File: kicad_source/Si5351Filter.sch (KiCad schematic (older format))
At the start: 31 parts, among them CN1 CON-SMA-EDGE-S-ND, CN2 CON-SMA-EDGE-S-ND, CN3 CON-SMA-EDGE-S-ND, CN4 CON-SMA-EDGE-S-ND, CN5 CON-SMA-EDGE-S-ND, CN6 CON-SMA-EDGE-S-ND

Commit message: added dual footprint for big and small SMA connectors
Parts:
- CN1, CN2, CN3, CN4, CN5, CN6: footprint CON_wuerth:WR-SMA-PCB -> CON_wuerth:WR-SMA-PCB_dual
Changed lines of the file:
@@
 F 0 "CN2" H 6572 1575 60  0000 R CNN
 F 1 "CON-SMA-EDGE-S-ND " H 6572 1469 60  0000 R CNN
-F 2 "CON_wuerth:WR-SMA-PCB" H 6572 1469 60  0001 R CNN
+F 2 "CON_wuerth:WR-SMA-PCB_dual" H 6572 1469 60  0001 R CNN
 F 3 "" H 7200 1500 60  0000 C CNN
 	1    7200 1500
@@
 F 0 "CN4" H 6572 2925 60  0000 R CNN
 F 1 "CON-SMA-EDGE-S-ND " H 6572 2819 60  0000 R CNN
-F 2 "CON_wuerth:WR-SMA-PCB" H 6572 2819 60  0001 R CNN
+F 2 "CON_wuerth:WR-SMA-PCB_dual" H 6572 2819 60  0001 R CNN
 F 3 "" H 7200 2850 60  0000 C CNN
 	1    7200 2850
@@
 F 0 "CN1" H 2222 1575 60  0000 R CNN
 F 1 "CON-SMA-EDGE-S-ND " H 2222 1469 60  0000 R CNN
-F 2 "CON_wuerth:WR-SMA-PCB" H 2222 1469 60  0001 R CNN
+F 2 "CON_wuerth:WR-SMA-PCB_dual" H 2222 1469 60  0001 R CNN
 F 3 "" H 2850 1500 60  0000 C CNN
 	1    2850 1500
@@
 F 0 "CN3" H 2222 2925 60  0000 R CNN
 F 1 "CON-SMA-EDGE-S-ND " H 2222 2819 60  0000 R CNN
-F 2 "CON_wuerth:WR-SMA-PCB" H 2222 2819 60  0001 R CNN
+F 2 "CON_wuerth:WR-SMA-PCB_dual" H 2222 2819 60  0001 R CNN
 F 3 "" H 2850 2850 60  0000 C CNN
 	1    2850 2850
@@
 F 0 "CN6" H 6572 4175 60  0000 R CNN
 F 1 "CON-SMA-EDGE-S-ND " H 6572 4069 60  0000 R CNN
-F 2 "CON_wuerth:WR-SMA-PCB" H 6572 4069 60  0001 R CNN
+F 2 "CON_wuerth:WR-SMA-PCB_dual" H 6572 4069 60  0001 R CNN
 F 3 "" H 7200 4100 60  0000 C CNN
 	1    7200 4100
@@
 F 0 "CN5" H 2222 4175 60  0000 R CNN
 F 1 "CON-SMA-EDGE-S-ND " H 2222 4069 60  0000 R CNN
-F 2 "CON_wuerth:WR-SMA-PCB" H 2222 4069 60  0001 R CNN
+F 2 "CON_wuerth:WR-SMA-PCB_dual" H 2222 4069 60  0001 R CNN
 F 3 "" H 2850 4100 60  0000 C CNN
 	1    2850 4100

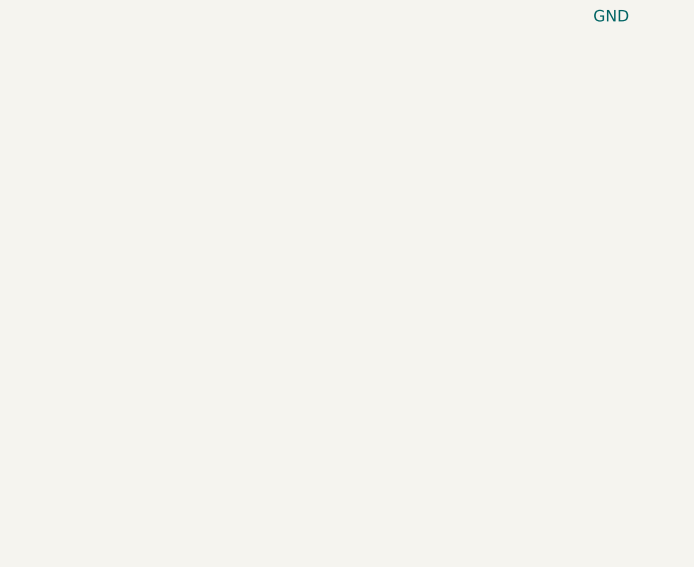
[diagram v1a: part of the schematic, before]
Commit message: added holes for mounting and grounding
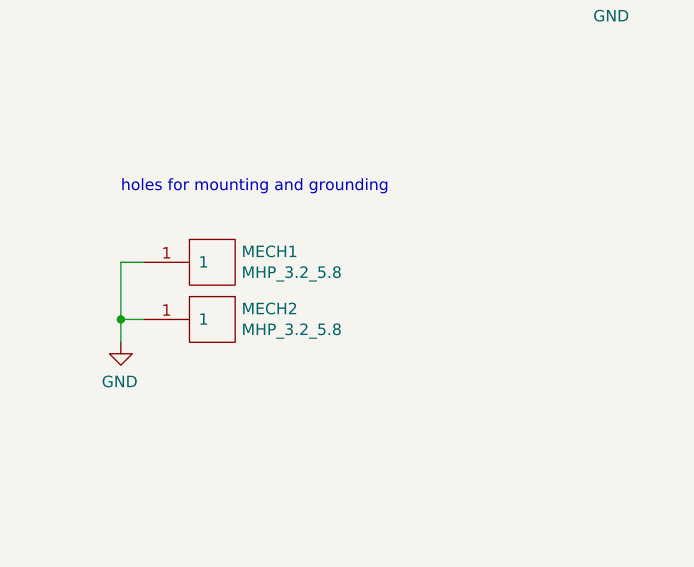
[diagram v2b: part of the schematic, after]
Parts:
- added MECH1, MECH2: MHP_3.2_5.8, MECH_mounting_holes:MHP_3.2_5.8, symbol MECH_mounting-holes:MHP_3.2_5.8
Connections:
- net GND: now also MECH1.1, MECH2.1
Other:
- note added: "holes for mounting and grounding"
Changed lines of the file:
@@
 Wire Wire Line
 	3050 4100 3950 4100
+$Comp
+L MECH_mounting-holes:MHP_3.2_5.8 MECH1
+U 1 1 611EB9B8
+P 1350 5700
+F 0 "MECH1" H 1478 5746 50  0000 L CNN
+F 1 "MHP_3.2_5.8" H 1478 5655 50  0000 L CNN
+F 2 "MECH_mounting_holes:MHP_3.2_5.8" H 1250 5750 50  0001 C CNN
+F 3 "" H 1350 5700 50  0001 C CNN
+	1    1350 5700
+	1    0    0    -1
+$EndComp
+$Comp
+L MECH_mounting-holes:MHP_3.2_5.8 MECH2
+U 1 1 611EC658
+P 1350 5950
+F 0 "MECH2" H 1478 5996 50  0000 L CNN
+F 1 "MHP_3.2_5.8" H 1478 5905 50  0000 L CNN
+F 2 "MECH_mounting_holes:MHP_3.2_5.8" H 1250 6000 50  0001 C CNN
+F 3 "" H 1350 5950 50  0001 C CNN
+	1    1350 5950
+	1    0    0    -1
+$EndComp
+$Comp
+L power-supply:GND #PWR019
+U 1 1 611EC8B2
+P 950 6050
+F 0 "#PWR019" H 950 5800 50  0001 C CNN
+F 1 "GND" H 955 5877 50  0000 C CNN
+F 2 "" H 950 6050 50  0000 C CNN
+F 3 "" H 950 6050 50  0000 C CNN
+	1    950  6050
+	-1   0    0    -1
+$EndComp
+Wire Wire Line
+	1050 5700 950  5700
+Wire Wire Line
+	950  5700 950  5950
+Wire Wire Line
+	1050 5950 950  5950
+Connection ~ 950  5950
+Wire Wire Line
+	950  5950 950  6050
+Text Notes 950  5400 0    50   ~ 0
+holes for mounting and grounding
 $EndSCHEMATC
